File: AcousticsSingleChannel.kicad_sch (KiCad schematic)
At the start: 18 parts, among them J1 SSW-104-01-G-D, J2 TSW-104-07-F-D, U2 OPA1604AIPWR, U4 ADS7042IDCUR

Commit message: Ready for Review.
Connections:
- net at R26.1, R27.2: now also J2.06; no longer J2.05
- net DOUT: now reaches R26.2, U4.3 (SDO)
- net at U4.2 (SCLK): now also J2.03; no longer J2.07
- net at U4.4 (CS_N): now also J2.01; no longer J2.03
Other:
- moved on the sheet: R26, R27
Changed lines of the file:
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@@
+	)
+	(junction
+		(at 115.57 149.86)
+		(diameter 0)
+		(color 0 0 0 0)
 	)
 	(junction
@@
 	)
 	(junction
-		(at 182.88 149.86)
-		(diameter 0)
-		(color 0 0 0 0)
-	)
-	(junction
 		(at 243.84 101.6)
 		(diameter 0)
@@
 	)
 	(no_connect
-		(at 146.05 149.86)
+		(at 171.45 147.32)
+	)
+	(no_connect
+		(at 171.45 149.86)
 	)
 	(no_connect
@@
 		(at 146.05 154.94)
 	)
-	(no_connect
-		(at 171.45 154.94)
+	(wire
+		(pts
+			(xy 220.98 152.4) (xy 171.45 152.4)
+		)
+		(stroke
+			(width 0)
+			(type default)
+		)
+	)
+	(wire
+		(pts
+			(xy 232.41 149.86) (xy 241.3 149.86)
+		)
+		(stroke
+			(width 0)
+			(type default)
+		)
 	)
 	(wire
@@
 	(wire
 		(pts
-			(xy 182.88 149.86) (xy 182.88 151.13)
-		)
-		(stroke
-			(width 0)
-			(type default)
-		)
-	)
-	(wire
-		(pts
 			(xy 34.29 96.52) (xy 55.88 96.52)
 		)
@@
 	(wire
 		(pts
-			(xy 176.53 143.51) (xy 238.76 143.51)
-		)
-		(stroke
-			(width 0)
-			(type default)
-		)
-	)
-	(wire
-		(pts
 			(xy 241.3 137.16) (xy 241.3 149.86)
 		)
@@
 	(wire
 		(pts
-			(xy 176.53 147.32) (xy 171.45 147.32)
-		)
-		(stroke
-			(width 0)
-			(type default)
-		)
-	)
-	(wire
-		(pts
 			(xy 68.58 111.76) (xy 72.39 111.76)
 		)
@@
 	(wire
 		(pts
-			(xy 172.72 166.37) (xy 243.84 166.37)
-		)
-		(stroke
-			(width 0)
-			(type default)
-		)
-	)
-	(wire
-		(pts
 			(xy 161.29 111.76) (xy 149.86 111.76)
 		)
@@
 	(wire
 		(pts
-			(xy 241.3 149.86) (xy 195.58 149.86)
+			(xy 102.87 149.86) (xy 93.98 149.86)
+		)
+		(stroke
+			(width 0)
+			(type default)
+		)
+	)
+	(wire
+		(pts
+			(xy 220.98 143.51) (xy 220.98 152.4)
 		)
 		(stroke
@@
 	(wire
 		(pts
+			(xy 113.03 149.86) (xy 115.57 149.86)
+		)
+		(stroke
+			(width 0)
+			(type default)
+		)
+	)
+	(wire
+		(pts
 			(xy 210.82 93.98) (xy 214.63 93.98)
 		)
@@
 	(wire
 		(pts
-			(xy 171.45 149.86) (xy 182.88 149.86)
-		)
-		(stroke
-			(width 0)
-			(type default)
-		)
-	)
-	(wire
-		(pts
 			(xy 20.32 111.76) (xy 35.56 111.76)
 		)
@@
 	(wire
 		(pts
-			(xy 243.84 166.37) (xy 243.84 137.16)
-		)
-		(stroke
-			(width 0)
-			(type default)
-		)
-	)
-	(wire
-		(pts
-			(xy 176.53 143.51) (xy 176.53 147.32)
-		)
-		(stroke
-			(width 0)
-			(type default)
-		)
-	)
-	(wire
-		(pts
-			(xy 185.42 149.86) (xy 182.88 149.86)
+			(xy 243.84 154.94) (xy 243.84 137.16)
 		)
 		(stroke
@@
 	(wire
 		(pts
-			(xy 171.45 152.4) (xy 172.72 152.4)
-		)
-		(stroke
-			(width 0)
-			(type default)
-		)
-	)
-	(wire
-		(pts
 			(xy 52.07 46.99) (xy 54.61 46.99)
 		)
@@
 	(wire
 		(pts
+			(xy 238.76 143.51) (xy 220.98 143.51)
+		)
+		(stroke
+			(width 0)
+			(type default)
+		)
+	)
+	(wire
+		(pts
 			(xy 214.63 93.98) (xy 228.6 93.98)
 		)
@@
 	(wire
 		(pts
-			(xy 172.72 152.4) (xy 172.72 166.37)
-		)
-		(stroke
-			(width 0)
-			(type default)
-		)
-	)
-	(wire
-		(pts
 			(xy 196.85 121.92) (xy 196.85 119.38)
 		)
@@
 	(wire
 		(pts
+			(xy 171.45 154.94) (xy 243.84 154.94)
+		)
+		(stroke
+			(width 0)
+			(type default)
+		)
+	)
+	(wire
+		(pts
 			(xy 49.53 45.72) (xy 52.07 45.72)
+		)
+		(stroke
+			(width 0)
+			(type default)
+		)
+	)
+	(wire
+		(pts
+			(xy 115.57 149.86) (xy 146.05 149.86)
 		)
 		(stroke
@@
 		)
 	)
+	(label "DOUT"
+		(at 232.41 149.86 180)
+		(effects
+			(font
+				(size 1.27 1.27)
+			)
+			(justify right bottom)
+		)
+	)
 	(label "G1_out"
 		(at 20.32 43.18 180)
@@
 			)
 			(justify left bottom)
+		)
+	)
+	(label "DOUT"
+		(at 93.98 149.86 180)
+		(effects
+			(font
+				(size 1.27 1.27)
+			)
+			(justify right bottom)
 		)
 	)
@@
 	(symbol
 		(lib_id "power:GND")
-		(at 182.88 161.29 0)
+		(at 115.57 160.02 0)
 		(unit 1)
 		(exclude_from_sim no)
@@
 		(dnp no)
 		(property "Reference" "#PWR017"
-			(at 182.88 167.64 0)
+			(at 115.57 166.37 0)
 			(effects
 				(font
@@
 		)
 		(property "Value" "GND"
-			(at 186.436 164.592 0)
+			(at 119.126 163.322 0)
 			(effects
 				(font
@@
 		)
 		(property "Footprint" ""
-			(at 182.88 161.29 0)
+			(at 115.57 160.02 0)
 			(effects
 				(font
@@
 		)
 		(property "Datasheet" ""
-			(at 182.88 161.29 0)
+			(at 115.57 160.02 0)
 			(effects
 				(font
@@
 		)
 		(property "Description" "Power symbol creates a global label with name \"GND\" , ground"
-			(at 182.88 161.29 0)
+			(at 115.57 160.02 0)
 			(effects
 				(font
@@
 	(symbol
 		(lib_id "AcousticsSingleChannel-altium-import:root_0_ERJ-3EKF7500V")
-		(at 190.5 149.86 0)
+		(at 107.95 149.86 180)
 		(unit 1)
 		(exclude_from_sim no)
@@
 		(dnp no)
 		(property "Reference" "R26"
-			(at 187.706 148.844 0)
+			(at 110.744 150.876 0)
 			(effects
 				(font
@@
 		)
 		(property "Value" "0"
-			(at 187.706 153.162 0)
-			(effects
-				(font
-					(size 1.27 1.27)
-				)
-				(justify left bottom)
+			(at 107.442 147.574 0)
+			(effects
+				(font
+					(size 1.27 1.27)
+				)
+				(justify right bottom)
 			)
 		)
 		(property "Footprint" "AltiumImports:SMD-0603-RES"
-			(at 190.5 149.86 0)
+			(at 107.95 149.86 0)
 			(effects
 				(font
@@
 		)
 		(property "Datasheet" ""
-			(at 190.5 149.86 0)
+			(at 107.95 149.86 0)
 			(effects
 				(font
@@
 		)
 		(property "Description" ""
-			(at 190.5 149.86 0)
+			(at 107.95 149.86 0)
 			(effects
 				(font
@@
 		)
 		(property "Part Number" "ERJ-3EKF7500V"
-			(at 190.5 149.86 0)
+			(at 107.95 149.86 0)
 			(effects
 				(font
@@
 	(symbol
 		(lib_id "AcousticsSingleChannel-altium-import:root_1_ERJ-3EKF1001V")
-		(at 182.88 156.21 0)
+		(at 115.57 154.94 0)
 		(unit 1)
 		(exclude_from_sim no)
@@
 		(dnp yes)
 		(property "Reference" "R27"
-			(at 183.642 155.956 0)
+			(at 116.332 154.686 0)
 			(effects
 				(font
@@
 		)
 		(property "Value" "0"
-			(at 183.642 158.496 0)
+			(at 116.332 157.226 0)
 			(effects
 				(font
@@
 		)
 		(property "Footprint" "AltiumImports:SMD-0603-RES"
-			(at 182.88 156.21 0)
+			(at 115.57 154.94 0)
 			(effects
 				(font
@@
 		)
 		(property "Datasheet" ""
-			(at 182.88 156.21 0)
+			(at 115.57 154.94 0)
 			(effects
 				(font
@@
 		)
 		(property "Description" ""
-			(at 182.88 156.21 0)
+			(at 115.57 154.94 0)
 			(effects
 				(font
@@
 		)
 		(property "Part Number" "ERJ-3EKF1001V"
-			(at 182.88 156.21 0)
-			(effects
-				(font
+			(at 115.57 154.94 0)
+			(effects
+				(font

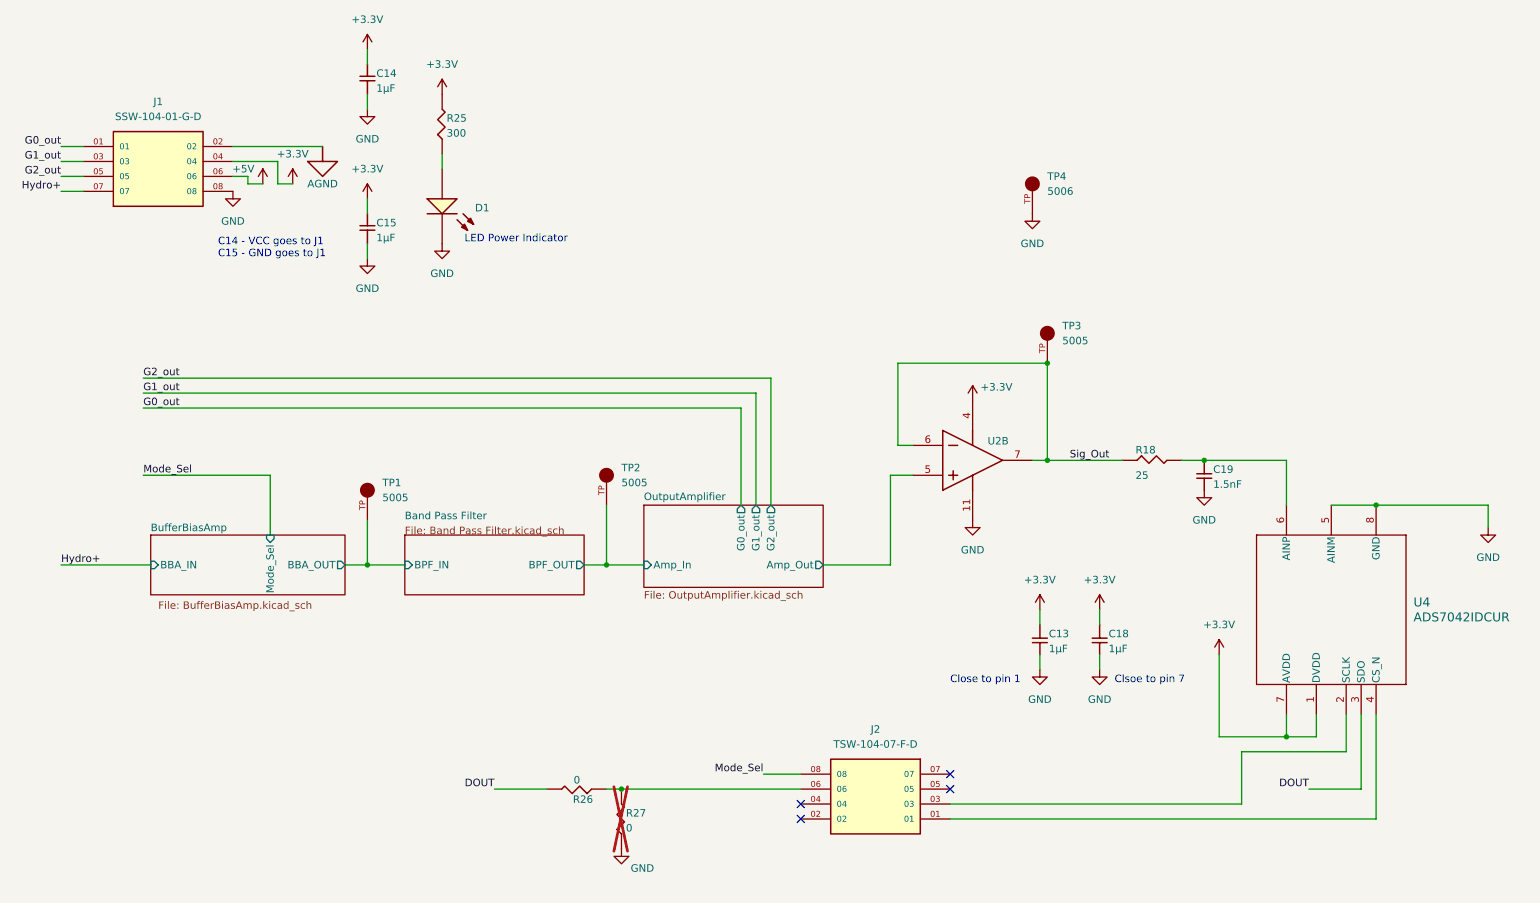
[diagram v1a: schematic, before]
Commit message: Changed headers.
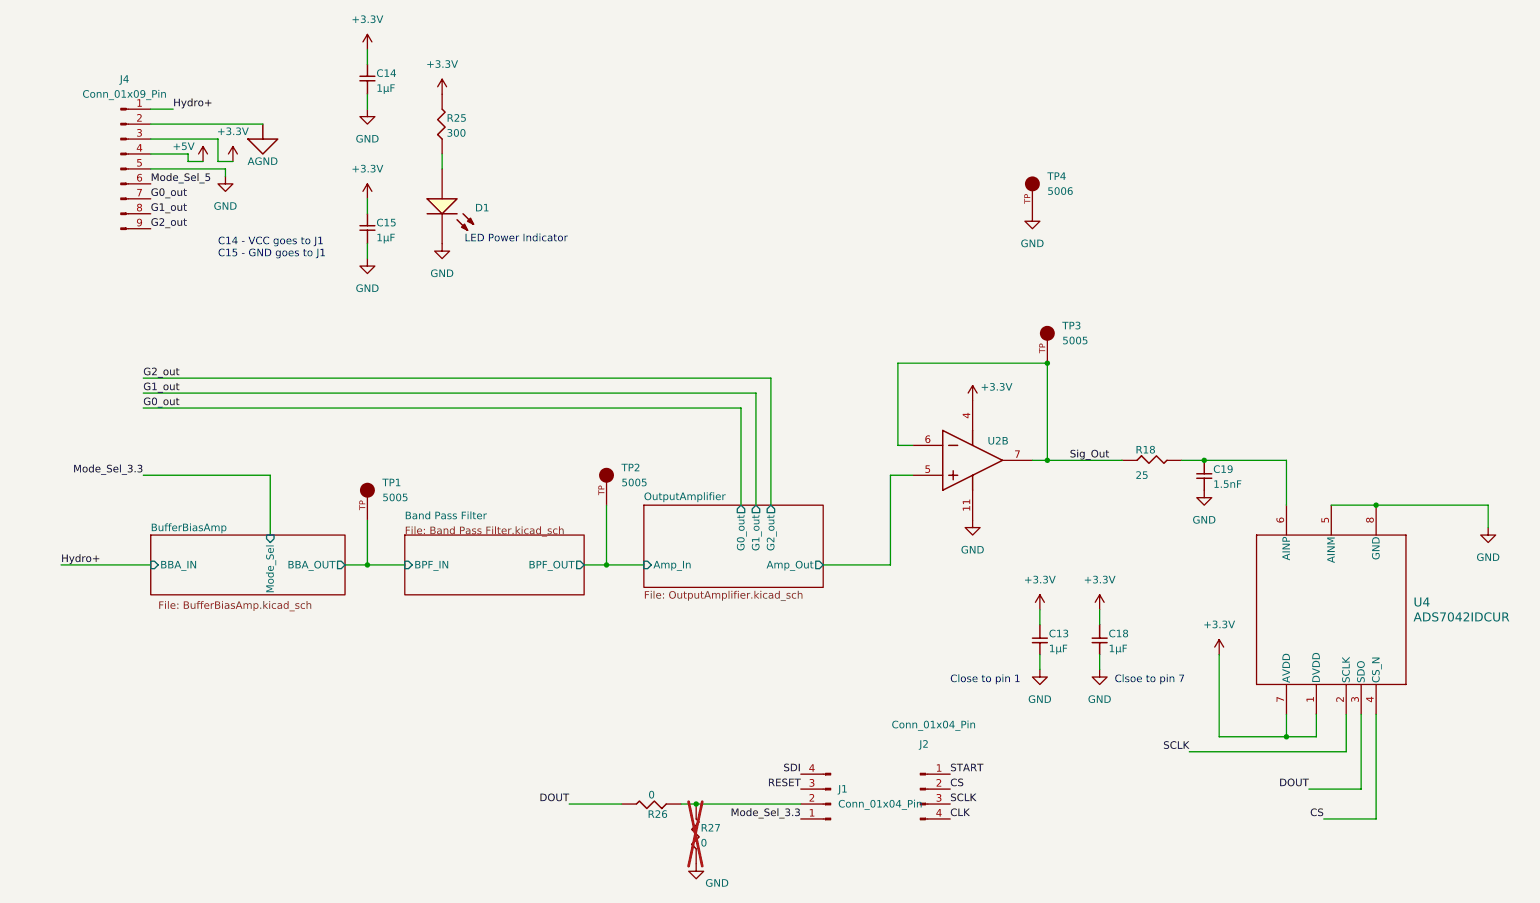
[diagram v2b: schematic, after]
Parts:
- removed J1: SSW-104-01-G-D, Accoustics:SAMTEC_SSW-104-01-G-D, symbol Accoustics:SSW-104-01-G-D
- removed J2: TSW-104-07-F-D, Accoustics:SAMTEC_TSW-104-07-F-D, symbol Accoustics:TSW-104-07-F-D
- added J1, J2: Conn_01x04_Pin, Connector_PinHeader_2.54mm:PinHeader_1x04_P2.54mm_Vertical, symbol Connector:Conn_01x04_Pin
- added J4: Conn_01x09_Pin, Connector_PinHeader_2.54mm:PinHeader_1x09_P2.54mm_Vertical, symbol Connector:Conn_01x09_Pin
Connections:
- net +3.3V: now also J4.3 (Pin_3)
- net +5V: now also J4.4 (Pin_4)
- net AGND: now also J4.2 (Pin_2)
- net G0_out: now also J4.7 (Pin_7)
- net G1_out: now also J4.8 (Pin_8)
- net G2_out: now also J4.9 (Pin_9)
- net GND: now also J4.5 (Pin_5)
- net Hydro+: now also J4.1 (Pin_1)
- net at R26.1, R27.2: now also J1.2 (Pin_2)
- net SCLK: now reaches U4.2 (SCLK)
- net SCLK: now also J2.3 (Pin_3)
- net CS: now reaches U4.4 (CS_N)
- net CS: now also J2.2 (Pin_2)
- new net CLK: J2.4 (Pin_4)
- new net Mode_Sel_3.3: J1.1 (Pin_1)
- new net Mode_Sel_5: J4.6 (Pin_6)
- new net RESET: J1.3 (Pin_3)
- new net SDI: J1.4 (Pin_4)
- new net START: J2.1 (Pin_1)
- no-connect marks 4 -> 0
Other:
- moved on the sheet: R26, R27

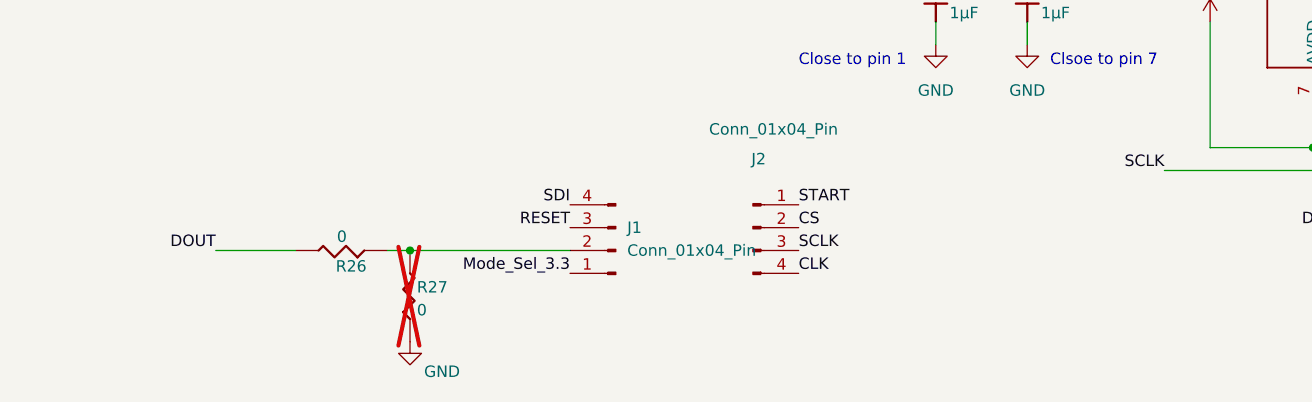
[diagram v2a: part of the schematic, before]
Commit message: Changed pinouts causing minor changes to layer1 layout.
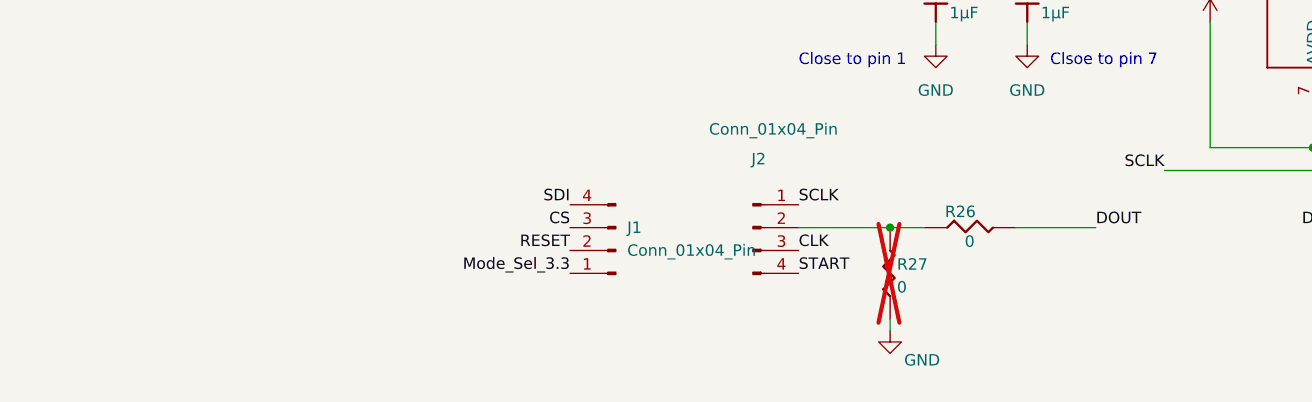
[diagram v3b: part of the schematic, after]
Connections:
- net CLK: now also J2.3 (Pin_3); no longer J2.4 (Pin_4)
- net CS: now also J1.3 (Pin_3); no longer J2.2 (Pin_2)
- net RESET: now also J1.2 (Pin_2); no longer J1.3 (Pin_3)
- net SCLK: now also J2.1 (Pin_1); no longer J2.3 (Pin_3)
- net START: now also J2.4 (Pin_4); no longer J2.1 (Pin_1)
- net at R26.1, R27.2: now also J2.2 (Pin_2); no longer J1.2 (Pin_2)
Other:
- moved on the sheet: R26, R27
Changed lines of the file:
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@@
+	)
+	(junction
+		(at 181.61 149.86)
+		(diameter 0)
+		(color 0 0 0 0)
 	)
 	(junction
@@
 		(color 0 0 0 0)
 	)
-	(junction
-		(at 128.27 152.4)
-		(diameter 0)
-		(color 0 0 0 0)
-	)
 	(wire
 		(pts
@@
 	(wire
 		(pts
+			(xy 171.45 149.86) (xy 181.61 149.86)
+		)
+		(stroke
+			(width 0)
+			(type default)
+		)
+	)
+	(wire
+		(pts
 			(xy 243.84 101.6) (xy 262.89 101.6)
 		)
@@
 	(wire
 		(pts
+			(xy 181.61 149.86) (xy 185.42 149.86)
+		)
+		(stroke
+			(width 0)
+			(type default)
+		)
+	)
+	(wire
+		(pts
 			(xy 161.29 111.76) (xy 149.86 111.76)
 		)
@@
 	(wire
 		(pts
+			(xy 181.61 161.29) (xy 181.61 160.02)
+		)
+		(stroke
+			(width 0)
+			(type default)
+		)
+	)
+	(wire
+		(pts
 			(xy 109.22 111.76) (xy 113.03 111.76)
 		)
@@
 	(wire
 		(pts
-			(xy 115.57 152.4) (xy 106.68 152.4)
+			(xy 195.58 149.86) (xy 204.47 149.86)
 		)
 		(stroke
@@
 	(wire
 		(pts
-			(xy 125.73 152.4) (xy 128.27 152.4)
-		)
-		(stroke
-			(width 0)
-			(type default)
-		)
-	)
-	(wire
-		(pts
 			(xy 210.82 93.98) (xy 214.63 93.98)
 		)
@@
 		(pts
 			(xy 135.89 85.09) (xy 135.89 101.6)
-		)
-		(stroke
-			(width 0)
-			(type default)
-		)
-	)
-	(wire
-		(pts
-			(xy 128.27 152.4) (xy 146.05 152.4)
 		)
 		(stroke
@@
 		)
 	)
-	(label "CS"
-		(at 171.45 149.86 0)
-		(effects
-			(font
-				(size 1.27 1.27)
-			)
-			(justify left bottom)
-		)
-	)
 	(label "Hydro+"
 		(at 39.37 34.29 0)
@@
 		)
 	)
+	(label "RESET"
+		(at 146.05 152.4 180)
+		(effects
+			(font
+				(size 1.27 1.27)
+			)
+			(justify right bottom)
+		)
+	)
 	(label "Sig_Out"
 		(at 191.77 93.98 0)
@@
 	)
 	(label "START"
-		(at 171.45 147.32 0)
+		(at 171.45 154.94 0)
 		(effects
 			(font
@@
 		)
 	)
-	(label "RESET"
+	(label "CS"
 		(at 146.05 149.86 180)
 		(effects
@@
 		)
 	)
-	(label "CLK"
-		(at 171.45 154.94 0)
+	(label "SCLK"
+		(at 171.45 147.32 0)
 		(effects
 			(font
@@
 		)
 	)
+	(label "CLK"
+		(at 171.45 152.4 0)
+		(effects
+			(font
+				(size 1.27 1.27)
+			)
+			(justify left bottom)
+		)
+	)
 	(label "G1_out"
 		(at 34.29 82.55 0)
@@
 		)
 	)
-	(label "SCLK"
-		(at 171.45 152.4 0)
-		(effects
-			(font
-				(size 1.27 1.27)
-			)
-			(justify left bottom)
-		)
-	)
 	(label "Hydro+"
 		(at 20.32 111.76 0)
@@
 	)
 	(label "DOUT"
-		(at 106.68 152.4 180)
+		(at 204.47 149.86 0)
 		(effects
 			(font
 				(size 1.27 1.27)
 			)
-			(justify right bottom)
+			(justify left bottom)
 		)
 	)
@@
 	(symbol
 		(lib_id "power:GND")
-		(at 128.27 162.56 0)
+		(at 181.61 161.29 0)
 		(unit 1)
 		(exclude_from_sim no)
@@
 		(dnp no)
 		(property "Reference" "#PWR017"
-			(at 128.27 168.91 0)
+			(at 181.61 167.64 0)
 			(effects
 				(font
@@
 		)
 		(property "Value" "GND"
-			(at 131.826 165.862 0)
+			(at 185.166 164.592 0)
 			(effects
 				(font
@@
 		)
 		(property "Footprint" ""
-			(at 128.27 162.56 0)
+			(at 181.61 161.29 0)
 			(effects
 				(font
@@
 		)
 		(property "Datasheet" ""
-			(at 128.27 162.56 0)
+			(at 181.61 161.29 0)
 			(effects
 				(font
@@
 		)
 		(property "Description" "Power symbol creates a global label with name \"GND\" , ground"
-			(at 128.27 162.56 0)
+			(at 181.61 161.29 0)
 			(effects
 				(font
@@
 	(symbol
 		(lib_id "AcousticsSingleChannel-altium-import:root_0_ERJ-3EKF7500V")
-		(at 120.65 152.4 180)
+		(at 190.5 149.86 0)
 		(unit 1)
 		(exclude_from_sim no)
@@
 		(dnp no)
 		(property "Reference" "R26"
-			(at 123.444 153.416 0)
+			(at 187.706 148.844 0)
 			(effects
 				(font
@@
 		)
 		(property "Value" "0"
-			(at 120.142 150.114 0)
+			(at 191.008 152.146 0)
 			(effects
 				(font
@@
 		)
 		(property "Footprint" "AltiumImports:SMD-0603-RES"
-			(at 120.65 152.4 0)
+			(at 190.5 149.86 0)
 			(effects
 				(font
@@
 		)
 		(property "Datasheet" ""
-			(at 120.65 152.4 0)
+			(at 190.5 149.86 0)
 			(effects
 				(font
@@
 		)
 		(property "Description" ""
-			(at 120.65 152.4 0)
+			(at 190.5 149.86 0)
 			(effects
 				(font
@@
 		)
 		(property "Part Number" "ERJ-3EKF7500V"
-			(at 120.65 152.4 0)
+			(at 190.5 149.86 0)
 			(effects
 				(font
@@
 	(symbol
 		(lib_id "AcousticsSingleChannel-altium-import:root_1_ERJ-3EKF1001V")
-		(at 128.27 157.48 0)
+		(at 181.61 154.94 0)
 		(unit 1)
 		(exclude_from_sim no)
@@
 		(dnp yes)
 		(property "Reference" "R27"
-			(at 129.032 157.226 0)
+			(at 182.372 154.686 0)
 			(effects
 				(font
@@
 		)
 		(property "Value" "0"
-			(at 129.032 159.766 0)
+			(at 182.372 157.226 0)
 			(effects
 				(font
@@
 		)
 		(property "Footprint" "AltiumImports:SMD-0603-RES"
-			(at 128.27 157.48 0)
+			(at 181.61 154.94 0)
 			(effects
 				(font
@@
 		)
 		(property "Datasheet" ""
-			(at 128.27 157.48 0)
+			(at 181.61 154.94 0)
 			(effects
 				(font
@@
 		)
 		(property "Description" ""
-			(at 128.27 157.48 0)
+			(at 181.61 154.94 0)
 			(effects
 				(font
@@
 		)
 		(property "Part Number" "ERJ-3EKF1001V"
-			(at 128.27 157.48 0)
-			(effects
-				(font
+			(at 181.61 154.94 0)
+			(effects
+				(font
